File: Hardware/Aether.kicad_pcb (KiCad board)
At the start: 2 copper layers, 66.5 x 26 mm, 83 parts, among them J1 PRGM, J2 CONN-2, J3 CONN-2, J4 CONN-2, J5 CONN-2, J6 CONN-3, J7 CONN-3, Q1 IRLML6401, U1 ANTENOVA-UB, U2 ADF7012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

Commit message: Prepare for fab
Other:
- board text added: "Aerodyne Labs Aether 1v0"
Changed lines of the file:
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@@
     (links 182)
     (no_connects 0)
-    (area 122.444023 93.0644 207.293981 122.9356)
+    (area 119.000002 90.150001 207.293981 125.2)
     (thickness 1.6)
-    (drawings 4)
+    (drawings 8)
     (tracks 579)
     (zones 0)
@@
     (nets 59)
   )
-  (page A3)
+  (page A4)
+  (title_block
+    (title "Aether - Pico Tracker")
+    (rev 1)
+    (company "Aerodyne Labs")
+    (comment 1 "Ethan Harstad - eharstad@aerodynelabs.com")
+  )
   (layers
     (15 F.Cu signal)
@@
     (19 F.Paste user)
     (20 B.SilkS user)
-    (21 F.SilkS user hide)
+    (21 F.SilkS user)
     (22 B.Mask user)
     (23 F.Mask user)
@@
     (mod_text_size 1 1)
     (mod_text_width 0.15)
-    (pad_size 1.5 1.5)
-    (pad_drill 0.6)
+    (pad_size 4.191 2.66446)
+    (pad_drill 0)
     (pad_to_mask_clearance 0)
-    (aux_axis_origin 0 0)
+    (aux_axis_origin 128.5 95)
     (visible_elements 7FFFFFBF)
     (pcbplotparams
-      (layerselection 3178497)
+      (layerselection 284721153)
       (usegerberextensions true)
       (excludeedgelayer true)
@@
       (viasonmask false)
       (mode 1)
-      (useauxorigin false)
+      (useauxorigin true)
       (hpglpennumber 1)
       (hpglpenspeed 20)
@@
       (plotinvisibletext false)
       (padsonsilk false)
-      (subtractmaskfromsilk false)
+      (subtractmaskfromsilk true)
       (outputformat 1)
       (mirror false)
-      (drillshape 1)
+      (drillshape 0)
       (scaleselection 1)
-      (outputdirectory ""))
+      (outputdirectory Gerber/))
   )
   (net 0 "")
@@
     )
   )
-  (module SMA_Edge (layer F.Cu)
-    (at 194.5 115.5 180)
-    (descr "DK#: WM5536-ND")
-    (tags SMA)
-    (fp_text reference AE1 (at 10.20064 -2.60096 180) (layer F.SilkS) hide
-      (effects (font (size 1.524 1.524) (thickness 0.3048)))
-    )
-    (fp_text value ANTENNA (at 7.80034 2.99974 180) (layer F.SilkS) hide
-      (effects (font (size 1.524 1.524) (thickness 0.3048)))
-    )
-    (fp_line (start -1.00076 -3.2004) (end -12.40028 -3.2004) (layer Dwgs.User) (width 0.381))
-    (fp_line (start -12.40028 -3.2004) (end -12.40028 3.2004) (layer Dwgs.User) (width 0.381))
-    (fp_line (start -12.40028 3.2004) (end -1.00076 3.2004) (layer Dwgs.User) (width 0.381))
-    (fp_line (start 0 -3.2004) (end -1.00076 -3.2004) (layer Dwgs.User) (width 0.381))
-    (fp_line (start -1.00076 -3.2004) (end -1.00076 3.2004) (layer Dwgs.User) (width 0.381))
-    (fp_line (start -1.00076 3.2004) (end 0 3.2004) (layer Dwgs.User) (width 0.381))
-    (pad P smd rect (at 2.19964 0 180) (size 4.191 1.78054)
-      (layers F.Cu F.Paste F.Mask)
-      (net 37 N-000003)
-    )
-    (pad S smd rect (at 2.19964 -3.4925 180) (size 4.191 2.66446)
-      (layers F.Cu F.Paste F.Mask)
-      (net 32 GND)
-    )
-    (pad S smd rect (at 2.19964 3.4925 180) (size 4.191 2.66446)
-      (layers *.Paste *.Mask F.Cu)
-      (net 32 GND)
-    )
-    (pad S smd rect (at 2.2 -3.5 180) (size 4.191 2.66446)
-      (layers *.Paste *.Mask B.Cu)
-      (net 32 GND)
-    )
-    (pad S smd rect (at 2.2 3.5 180) (size 4.191 2.66446)
-      (layers *.Paste *.Mask B.Cu)
-      (net 32 GND)
-    )
-    (model 3D/Connectors/SMA_EDGE.wrl
-      (at (xyz 0 0 0))
-      (scale (xyz 10 10 10))
-      (rotate (xyz 0 0 0))
-    )
-  )
   (module RESC1608-N (layer F.Cu)
     (at 165.5 115.5 90)
@@
     )
   )
-  (module MECH-HOLE220 (layer F.Cu)
-    (at 130.5 97)
-    (fp_text reference MECH-HOLE220-1 (at 0 0) (layer F.SilkS) hide
-      (effects (font (size 1 1) (thickness 0.15)))
-    )
-    (fp_text value VAL** (at 0 0) (layer F.SilkS) hide
-      (effects (font (size 1 1) (thickness 0.15)))
-    )
-    (fp_circle (center 0 0) (end 2.5 0) (layer F.SilkS) (width 0.15))
-    (pad "" thru_hole circle (at 0 0) (size 2.8 2.8) (drill 2.2)
-      (layers *.Cu *.Mask F.SilkS)
-    )
-  )
   (module FIDUCIAL-1MM (layer F.Cu)
     (at 133.25 96.75)
@@
     )
   )
-  (module MECH-HOLE220 (layer F.Cu)
-    (at 193 97)
-    (fp_text reference MECH-HOLE220-2 (at 0 0) (layer F.SilkS) hide
-      (effects (font (size 1 1) (thickness 0.15)))
-    )
-    (fp_text value VAL** (at 0 0) (layer F.SilkS) hide
-      (effects (font (size 1 1) (thickness 0.15)))
-    )
-    (fp_circle (center 0 0) (end 2.5 0) (layer F.SilkS) (width 0.15))
-    (pad "" thru_hole circle (at 0 0) (size 2.8 2.8) (drill 2.2)
-      (layers *.Cu *.Mask F.SilkS)
-    )
-  )
   (module FIDUCIAL-1MM (layer F.Cu)
     (at 186.5 96.75)
@@
     )
   )
+  (module MECH-HOLE220 (layer F.Cu)
+    (at 193 97)
+    (fp_text reference MECH-HOLE220-2 (at 0 0) (layer F.SilkS) hide
+      (effects (font (size 1 1) (thickness 0.15)))
+    )
+    (fp_text value VAL** (at 0 0) (layer F.SilkS) hide
+      (effects (font (size 1 1) (thickness 0.15)))
+    )
+    (fp_circle (center 0 0) (end 2.5 0) (layer Dwgs.User) (width 0.15))
+    (pad "" thru_hole circle (at 0 0) (size 2.8 2.8) (drill 2.2)
+      (layers *.Cu *.Mask F.SilkS)
+    )
+  )
+  (module MECH-HOLE220 (layer F.Cu)
+    (at 130.5 97)
+    (fp_text reference MECH-HOLE220-1 (at 0 0) (layer F.SilkS) hide
+      (effects (font (size 1 1) (thickness 0.15)))
+    )
+    (fp_text value VAL** (at 0 0) (layer F.SilkS) hide
+      (effects (font (size 1 1) (thickness 0.15)))
+    )
+    (fp_circle (center 0 0) (end 2.5 0) (layer Dwgs.User) (width 0.15))
+    (pad "" thru_hole circle (at 0 0) (size 2.8 2.8) (drill 2.2)
+      (layers *.Cu *.Mask F.SilkS)
+    )
+  )
+  (module SMA_Edge (layer F.Cu)
+    (at 194.5 115.5 180)
+    (descr "DK#: WM5536-ND")
+    (tags SMA)
+    (fp_text reference AE1 (at 10.20064 -2.60096 180) (layer F.SilkS) hide
+      (effects (font (size 1.524 1.524) (thickness 0.3048)))
+    )
+    (fp_text value ANTENNA (at 7.80034 2.99974 180) (layer F.SilkS) hide
+      (effects (font (size 1.524 1.524) (thickness 0.3048)))
+    )
+    (fp_line (start -1.00076 -3.2004) (end -12.40028 -3.2004) (layer Dwgs.User) (width 0.381))
+    (fp_line (start -12.40028 -3.2004) (end -12.40028 3.2004) (layer Dwgs.User) (width 0.381))
+    (fp_line (start -12.40028 3.2004) (end -1.00076 3.2004) (layer Dwgs.User) (width 0.381))
+    (fp_line (start 0 -3.2004) (end -1.00076 -3.2004) (layer Dwgs.User) (width 0.381))
+    (fp_line (start -1.00076 -3.2004) (end -1.00076 3.2004) (layer Dwgs.User) (width 0.381))
+    (fp_line (start -1.00076 3.2004) (end 0 3.2004) (layer Dwgs.User) (width 0.381))
+    (pad P smd rect (at 2.19964 0 180) (size 4.191 1.78054)
+      (layers F.Cu F.Mask)
+      (net 37 N-000003)
+    )
+    (pad S smd rect (at 2.19964 -3.4925 180) (size 4.191 2.66446)
+      (layers F.Cu F.Mask)
+      (net 32 GND)
+    )
+    (pad S smd rect (at 2.19964 3.4925 180) (size 4.191 2.66446)
+      (layers *.Mask F.Cu)
+      (net 32 GND)
+    )
+    (pad S smd rect (at 2.2 -3.5 180) (size 4.191 2.66446)
+      (layers *.Mask B.Cu)
+      (net 32 GND)
+    )
+    (pad S smd rect (at 2.2 3.5 180) (size 4.191 2.66446)
+      (layers *.Mask B.Cu)
+      (net 32 GND)
+    )
+    (model 3D/Connectors/SMA_EDGE.wrl
+      (at (xyz 0 0 0))
+      (scale (xyz 10 10 10))
+      (rotate (xyz 0 0 0))
+    )
+  )
+  (dimension 62.5 (width 0.3) (layer Cmts.User)
+    (gr_text "62.500 mm" (at 161.75 91.650001) (layer Cmts.User)
+      (effects (font (size 1.5 1.5) (thickness 0.3)))
+    )
+    (feature1 (pts (xy 193 94) (xy 193 90.300001)))
+    (feature2 (pts (xy 130.5 94) (xy 130.5 90.300001)))
+    (crossbar (pts (xy 130.5 93.000001) (xy 193 93.000001)))
+    (arrow1a (pts (xy 193 93.000001) (xy 191.873497 93.586421)))
+    (arrow1b (pts (xy 193 93.000001) (xy 191.873497 92.413581)))
+    (arrow2a (pts (xy 130.5 93.000001) (xy 131.626503 93.586421)))
+    (arrow2b (pts (xy 130.5 93.000001) (xy 131.626503 92.413581)))
+  )
+  (dimension 26 (width 0.3) (layer Cmts.User)
+    (gr_text "26.000 mm" (at 125.650001 108 270) (layer Cmts.User)
+      (effects (font (size 1.5 1.5) (thickness 0.3)))
+    )
+    (feature1 (pts (xy 128 121) (xy 124.300001 121)))
+    (feature2 (pts (xy 128 95) (xy 124.300001 95)))
+    (crossbar (pts (xy 127.000001 95) (xy 127.000001 121)))
+    (arrow1a (pts (xy 127.000001 121) (xy 126.413581 119.873497)))
+    (arrow1b (pts (xy 127.000001 121) (xy 127.586421 119.873497)))
+    (arrow2a (pts (xy 127.000001 95) (xy 126.413581 96.126503)))
+    (arrow2b (pts (xy 127.000001 95) (xy 127.586421 96.126503)))
+  )
+  (dimension 66.5 (width 0.3) (layer Cmts.User)
+    (gr_text "66.500 mm" (at 161.75 123.849999) (layer Cmts.User)
+      (effects (font (size 1.5 1.5) (thickness 0.3)))
+    )
+    (feature1 (pts (xy 195 121.5) (xy 195 125.199999)))
+    (feature2 (pts (xy 128.5 121.5) (xy 128.5 125.199999)))
+    (crossbar (pts (xy 128.5 122.499999) (xy 195 122.499999)))
+    (arrow1a (pts (xy 195 122.499999) (xy 193.873497 123.086419)))
+    (arrow1b (pts (xy 195 122.499999) (xy 193.873497 121.913579)))
+    (arrow2a (pts (xy 128.5 122.499999) (xy 129.626503 123.086419)))
+    (arrow2b (pts (xy 128.5 122.499999) (xy 129.626503 121.913579)))
+  )
+  (gr_text "Aerodyne Labs\nAether 1v0" (at 143.5 113) (layer B.SilkS)
+    (effects (font (size 1.5 1.5) (thickness 0.3)) (justify mirror))
+  )
   (gr_line (start 128.5 95) (end 128.5 121) (angle 90) (layer Edge.Cuts) (width 0.1))

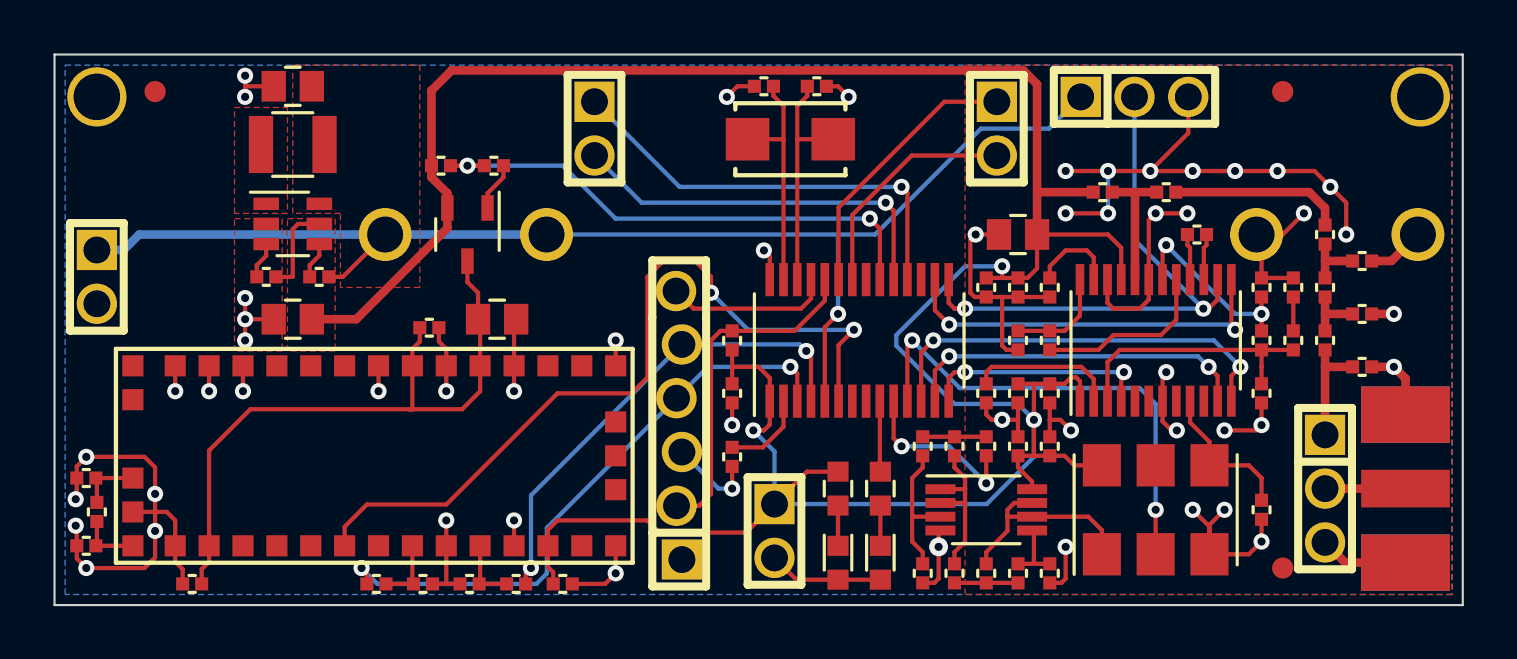
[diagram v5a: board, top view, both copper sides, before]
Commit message: Consolidate LED resistors
See #1
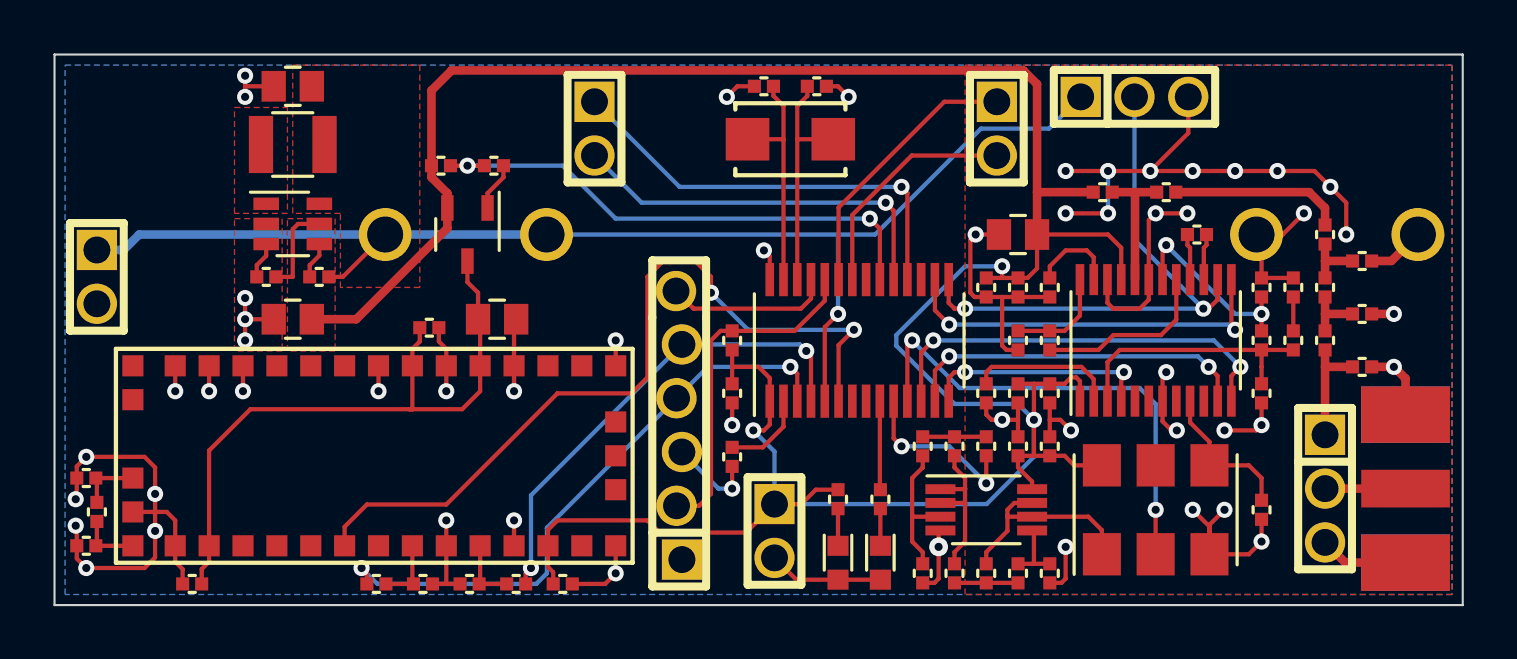
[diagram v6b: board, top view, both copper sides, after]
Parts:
- removed FIDUCIAL-1MM-1, FIDUCIAL-1MM-2, FIDUCIAL-1MM-3: VAL**, FIDUCIAL-1MM
- removed MECH-HOLE220-1, MECH-HOLE220-2: VAL**, MECH-HOLE220
- R1, R2: footprint RESC1608-N -> RESC1005-N
- R4: value 100 -> 120
- moved R1 0.50 mm to (167.5, 116.0)
- moved R2 0.50 mm to (165.5, 116.0)
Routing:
- net /Core/Stat: track 3.34 -> 4.19 mm

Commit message: Consolidate audio filter
Consolidate pull up resistors and audio filter.
Consolidate loop filter capacitor and audio filter.
See #1
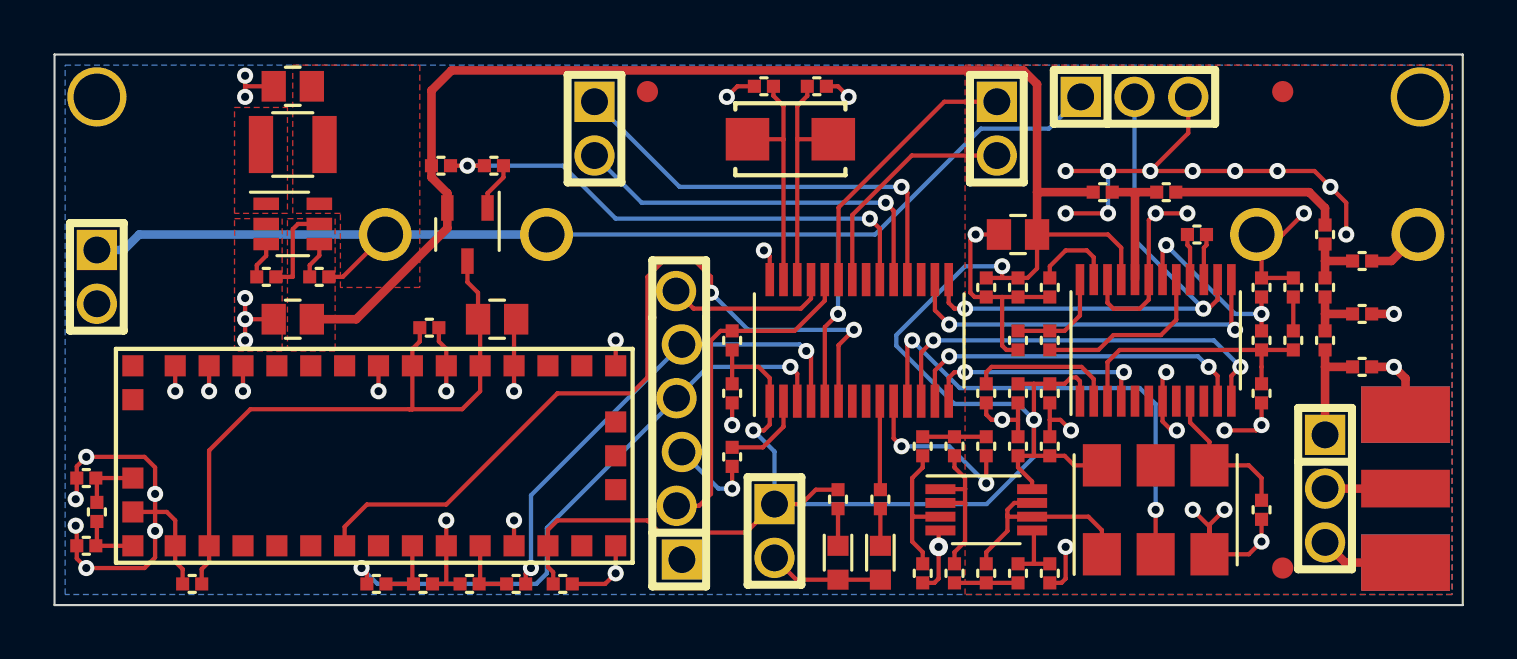
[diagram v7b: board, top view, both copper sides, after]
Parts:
- added FIDUCIAL-1MM-1: VAL**, FIDUCIAL-1MM, F.Cu at (186.5, 96.8)
- added FIDUCIAL-1MM-2: VAL**, FIDUCIAL-1MM, F.Cu at (186.5, 119.2)
- added FIDUCIAL-1MM-3: VAL**, FIDUCIAL-1MM, F.Cu at (156.5, 96.8)
- added MECH-HOLE220-1: VAL**, MECH-HOLE220, F.Cu at (130.5, 97.0)
- added MECH-HOLE220-2: VAL**, MECH-HOLE220, F.Cu at (193.0, 97.0)
- R10, R11, R12, R8: value 16k -> 10k

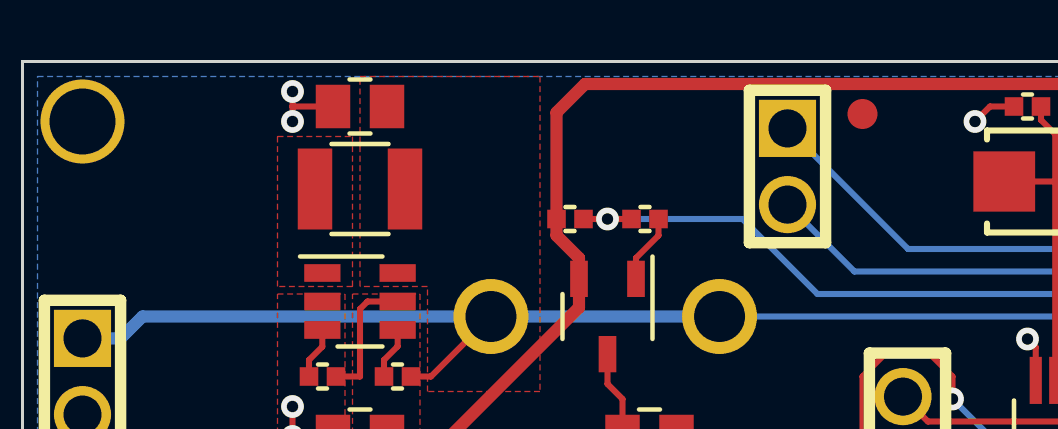
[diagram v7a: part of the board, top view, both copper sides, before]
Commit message: Re-add fiducials
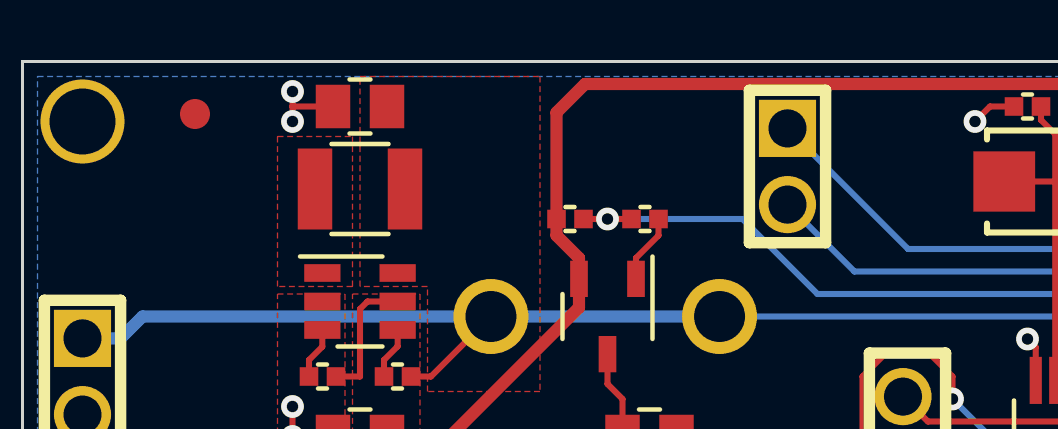
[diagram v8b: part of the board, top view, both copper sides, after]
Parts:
- moved FIDUCIAL-1MM-3 22.2 mm to (134.2, 96.8)
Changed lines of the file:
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@@
     )
   )
-  (module FIDUCIAL-1MM   locked (layer F.Cu)
-    (at 156.5 96.75)
+  (module FIDUCIAL-1MM (layer F.Cu)
+    (at 134.25 96.75)
     (fp_text reference FIDUCIAL-1MM-3 (at 0 -1.5) (layer F.SilkS) hide
       (effects (font (size 1 1) (thickness 0.15)))
